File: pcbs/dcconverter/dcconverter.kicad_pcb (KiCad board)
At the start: 4 copper layers, 160 x 100 mm, 52 parts, among them IC1 NCP7805TG, J1 190-9991, J2 Conn_01x01, J3 Conn_01x01, J4 146-8335, J5 Conn_01x01, J6 Conn_01x01, J7 483-8461, J8 483-8461, Q1 NGTB40N120FL2WG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

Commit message: Add power planes
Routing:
- added copper zone on In2.Cu, net Net-(C1-Pad2)
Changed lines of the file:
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@@
+    )
+  )
+  (zone (net 15) (net_name "Net-(F2-Pad1)") (layer In2.Cu) (hatch edge 0.508)
+    (connect_pads (clearance 0.5))
+    (min_thickness 0.25)
+    (fill yes (arc_segments 32) (thermal_gap 0.508) (thermal_bridge_width 0.508) (smoothing chamfer) (radius 1))
+    (polygon
+      (pts
+        (xy 106 77.5) (xy 99 77.5) (xy 99 84) (xy 105 89.5) (xy 130 90)
+        (xy 130 92.5) (xy 133 95.5) (xy 133 108.5) (xy 142 108.5) (xy 146 104.5)
+        (xy 146 93) (xy 151 93) (xy 151 114) (xy 92.5 114) (xy 92.5 71.5)
+        (xy 106 71.5)
+      )
+    )
+  )
+  (zone (net 1) (net_name "Net-(C1-Pad2)") (layer In2.Cu) (hatch edge 0.508)
+    (connect_pads (clearance 0.5))
+    (min_thickness 0.25)
+    (fill yes (arc_segments 32) (thermal_gap 0.508) (thermal_bridge_width 0.508) (smoothing chamfer) (radius 1))
+    (polygon
+      (pts
+        (xy 173.5 61.5) (xy 137.5 61.5) (xy 130 70) (xy 130 88) (xy 105.5 88)
+        (xy 100 83) (xy 100 78) (xy 107.5 78) (xy 107.5 70) (xy 101 70)
+        (xy 101 39.5) (xy 173.5 39.5)
+      )
     )
   )

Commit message: Add power planes
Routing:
- added copper zone on In2.Cu, net Net-(D1-Pad1)
- added copper zone on In2.Cu, net Net-(D5-Pad1)
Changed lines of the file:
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@@
+    )
+  )
+  (zone (net 9) (net_name "Net-(D1-Pad1)") (layer In2.Cu) (hatch edge 0.508)
+    (connect_pads (clearance 0.5))
+    (min_thickness 0.25)
+    (fill yes (arc_segments 32) (thermal_gap 0.508) (thermal_bridge_width 0.508) (smoothing chamfer) (radius 1))
+    (polygon
+      (pts
+        (xy 173.5 17) (xy 173.5 38) (xy 99.5 38) (xy 99.5 70) (xy 91 70)
+        (xy 91 74.5) (xy 82.5 74.5) (xy 82.5 39) (xy 91 39) (xy 91 16.5)
+      )
+    )
+  )
+  (zone (net 12) (net_name "Net-(D5-Pad1)") (layer In2.Cu) (hatch edge 0.508)
+    (connect_pads (clearance 0.5))
+    (min_thickness 0.25)
+    (fill yes (arc_segments 32) (thermal_gap 0.508) (thermal_bridge_width 0.508) (smoothing chamfer) (radius 1))
+    (polygon
+      (pts
+        (xy 90 37.5) (xy 64.5 37.5) (xy 64.5 16.5) (xy 89.5 16.5)
+      )
     )
   )

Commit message: Improve power planes
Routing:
- added copper zone on In1.Cu, net (none)
- added copper zone on In2.Cu, net Net-(C1-Pad1)
- added copper zone on In2.Cu, net Net-(F2-Pad2)
- removed copper zone on In1.Cu, net Net-(C1-Pad2)
- removed copper zone on In2.Cu, net Net-(C1-Pad2)
- removed copper zone on In2.Cu, net Net-(D5-Pad1)
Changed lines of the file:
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@@
     (user_trace_width 5)
     (trace_clearance 0.2)
-    (zone_clearance 0.508)
-    (zone_45_only no)
+    (zone_clearance 0.5)
+    (zone_45_only yes)
     (trace_min 0.2)
     (via_size 0.8)
@@
   (segment (start 15.72501 99.76101) (end 18.647601 102.683601) (width 1) (layer In2.Cu) (net 28))
   (segment (start 15.72501 65.77499) (end 15.72501 99.76101) (width 1) (layer In2.Cu) (net 28))
-  (zone (net 1) (net_name "Net-(C1-Pad2)") (layer In1.Cu) (hatch edge 0.508)
-    (connect_pads (clearance 0.508))
-    (min_thickness 0.254)
+  (zone (net 0) (net_name "") (layer In1.Cu) (hatch edge 0.508)
+    (connect_pads (clearance 0.5))
+    (min_thickness 0.25)
     (fill yes (arc_segments 32) (thermal_gap 0.508) (thermal_bridge_width 0.508) (smoothing chamfer) (radius 1))
     (polygon
       (pts
-        (xy 173.5 17) (xy 174 103) (xy 163 103) (xy 163 114) (xy 27 114)
-        (xy 27 103) (xy 16 103) (xy 16 27) (xy 27 27) (xy 27 16)
-      )
-    )
-  )
-  (zone (net 15) (net_name "Net-(F2-Pad1)") (layer In2.Cu) (hatch edge 0.508)
-    (connect_pads (clearance 0.508))
-    (min_thickness 0.254)
-    (fill yes (arc_segments 32) (thermal_gap 0.508) (thermal_bridge_width 0.508) (smoothing chamfer) (radius 1))
-    (polygon
-      (pts
-        (xy 173.5 64) (xy 174 103) (xy 152.5 103) (xy 152.5 92) (xy 143.5 92)
-        (xy 143.5 105.5) (xy 141 108) (xy 134.5 108) (xy 134.5 95) (xy 131.5 92)
-        (xy 131.5 71) (xy 138 63.5)
+        (xy 163 114) (xy 27 114) (xy 27 103) (xy 16 103) (xy 16 27)
+        (xy 27 27) (xy 27 16) (xy 163 16)
       )
     )
@@
     (polygon
       (pts
-        (xy 106 77.5) (xy 99 77.5) (xy 99 84) (xy 105 89.5) (xy 130 90)
-        (xy 130 92.5) (xy 133 95.5) (xy 133 108.5) (xy 142 108.5) (xy 146 104.5)
-        (xy 146 93) (xy 151 93) (xy 151 114) (xy 92.5 114) (xy 92.5 71.5)
-        (xy 106 71.5)
+        (xy 174 103) (xy 153 103) (xy 153 91) (xy 143.5 91) (xy 143.5 103)
+        (xy 131.5 103) (xy 131.5 67.5) (xy 174 67.5)
       )
     )
   )
-  (zone (net 1) (net_name "Net-(C1-Pad2)") (layer In2.Cu) (hatch edge 0.508)
+  (zone (net 14) (net_name "Net-(F2-Pad2)") (layer In2.Cu) (hatch edge 0.508)
     (connect_pads (clearance 0.5))
     (min_thickness 0.25)
@@
     (polygon
       (pts
-        (xy 173.5 61.5) (xy 137.5 61.5) (xy 130 70) (xy 130 88) (xy 105.5 88)
-        (xy 100 83) (xy 100 78) (xy 107.5 78) (xy 107.5 70) (xy 101 70)
-        (xy 101 39.5) (xy 173.5 39.5)
+        (xy 129.5 105) (xy 144.5 105) (xy 144.5 92.5) (xy 151.5 92.5) (xy 151.5 114)
+        (xy 89 114) (xy 89 92.5) (xy 129.5 92.5)
+      )
+    )
+  )
+  (zone (net 14) (net_name "Net-(F2-Pad2)") (layer In2.Cu) (hatch edge 0.508)
+    (connect_pads (clearance 0.5))
+    (min_thickness 0.25)
+    (fill yes (arc_segments 32) (thermal_gap 0.508) (thermal_bridge_width 0.508) (smoothing chamfer) (radius 1))
+    (polygon
+      (pts
+        (xy 99 83.5) (xy 129.5 83.5) (xy 129.5 92.5) (xy 89 92.5) (xy 89 75.5)
+        (xy 99 75.5)
+      )
+    )
+  )
+  (zone (net 2) (net_name "Net-(C1-Pad1)") (layer In2.Cu) (hatch edge 0.508)
+    (connect_pads (clearance 0.5))
+    (min_thickness 0.25)
+    (fill yes (arc_segments 32) (thermal_gap 0.508) (thermal_bridge_width 0.508) (smoothing chamfer) (radius 1))
+    (polygon
+      (pts
+        (xy 174 66) (xy 130 66) (xy 130 82.5) (xy 105.5 82.5) (xy 105.5 66)
+        (xy 111 60.5) (xy 111 40) (xy 174 40)
       )
     )
@@
     (polygon
       (pts
-        (xy 173.5 17) (xy 173.5 38) (xy 99.5 38) (xy 99.5 70) (xy 91 70)
-        (xy 91 74.5) (xy 82.5 74.5) (xy 82.5 39) (xy 91 39) (xy 91 16.5)
+        (xy 174 38.5) (xy 91.5 38.5) (xy 91.5 16) (xy 174 16)
       )
     )
   )
-  (zone (net 12) (net_name "Net-(D5-Pad1)") (layer In2.Cu) (hatch edge 0.508)
+  (zone (net 9) (net_name "Net-(D1-Pad1)") (layer In2.Cu) (hatch edge 0.508)
     (connect_pads (clearance 0.5))
     (min_thickness 0.25)
@@
     (polygon
       (pts
-        (xy 90 37.5) (xy 64.5 37.5) (xy 64.5 16.5) (xy 89.5 16.5)
+        (xy 104.5 72) (xy 85 72) (xy 85 38.5) (xy 104.5 38.5)
       )
     )
+  )
+  (zone (net 9) (net_name "Net-(D1-Pad1)") (layer In2.Cu) (hatch edge 0.508)
+    (connect_pads (clearance 0.5))
+    (min_thickness 0.25)
+    (fill yes (arc_segments 32) (thermal_gap 0.508) (thermal_bridge_width 0.508) (smoothing chamfer) (radius 1))
+    (polygon
+      (pts
+        (xy 109.5 59.5) (xy 104.5 64.5) (xy 104.5 38.5) (xy 109.5 38.5)
+      )
+    )

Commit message: Improve power planes
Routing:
- net Net-(R12-Pad1): track 126.5 -> 141.6 mm
- added copper zone on In1.Cu, net Net-(C1-Pad2)
- added copper zone on In2.Cu, net Net-(D5-Pad1)
- added copper zone on In2.Cu, net Net-(D5-Pad2)
- added copper zone on In2.Cu, net Net-(F1-Pad2)
- removed copper zone on In1.Cu, net (none)
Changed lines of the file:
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@@
     (thickness 1.6)
     (drawings 4)
-    (tracks 286)
+    (tracks 288)
     (zones 0)
     (modules 52)
@@
   )
   (setup
-    (last_trace_width 2)
+    (last_trace_width 1)
     (user_trace_width 1)
     (user_trace_width 2)
@@
   (segment (start 71.66 33) (end 71.5 33.16) (width 2) (layer B.Cu) (net 28))
   (segment (start 75.5 33) (end 71.66 33) (width 2) (layer B.Cu) (net 28))
-  (segment (start 71.5 33.16) (end 42.66 62) (width 1) (layer In2.Cu) (net 28))
-  (segment (start 19.5 62) (end 15.72501 65.77499) (width 1) (layer In2.Cu) (net 28))
-  (segment (start 42.66 62) (end 19.5 62) (width 1) (layer In2.Cu) (net 28))
   (segment (start 31.016399 102.683601) (end 32.58 101.12) (width 1) (layer In2.Cu) (net 28))
   (segment (start 29.289471 102.683601) (end 31.016399 102.683601) (width 1) (layer In2.Cu) (net 28))
@@
   (segment (start 15.72501 99.76101) (end 18.647601 102.683601) (width 1) (layer In2.Cu) (net 28))
   (segment (start 15.72501 65.77499) (end 15.72501 99.76101) (width 1) (layer In2.Cu) (net 28))
-  (zone (net 0) (net_name "") (layer In1.Cu) (hatch edge 0.508)
+  (segment (start 71.5 33.16) (end 71.5 59) (width 1) (layer In2.Cu) (net 28))
+  (segment (start 55.24227 59) (end 52.74227 61.5) (width 1) (layer In2.Cu) (net 28))
+  (segment (start 71.5 59) (end 55.24227 59) (width 1) (layer In2.Cu) (net 28))
+  (segment (start 20 61.5) (end 15.72501 65.77499) (width 1) (layer In2.Cu) (net 28))
+  (segment (start 52.74227 61.5) (end 20 61.5) (width 1) (layer In2.Cu) (net 28))
+  (zone (net 1) (net_name "Net-(C1-Pad2)") (layer In1.Cu) (hatch edge 0.508)
     (connect_pads (clearance 0.5))
     (min_thickness 0.25)
@@
     (polygon
       (pts
-        (xy 163 114) (xy 27 114) (xy 27 103) (xy 16 103) (xy 16 27)
-        (xy 27 27) (xy 27 16) (xy 163 16)
+        (xy 174 103) (xy 163 103) (xy 163 114) (xy 27 114) (xy 27 103)
+        (xy 16 103) (xy 16 27) (xy 27 27) (xy 27 16) (xy 174 16)
       )
     )
@@
       )
     )
+  )
+  (zone (net 13) (net_name "Net-(F1-Pad2)") (layer In2.Cu) (hatch edge 0.508)
+    (connect_pads (clearance 0.5))
+    (min_thickness 0.25)
+    (fill yes (arc_segments 32) (thermal_gap 0.508) (thermal_bridge_width 0.508) (smoothing chamfer) (radius 1))
+    (polygon
+      (pts
+        (xy 47.5 59.5) (xy 16 59.5) (xy 16 27) (xy 27 27) (xy 27 16)
+        (xy 47.5 16)
+      )
+    )
+  )
+  (zone (net 12) (net_name "Net-(D5-Pad1)") (layer In2.Cu) (hatch edge 0.508)
+    (connect_pads (clearance 0.5))
+    (min_thickness 0.25)
+    (fill yes (arc_segments 32) (thermal_gap 0.508) (thermal_bridge_width 0.508) (smoothing chamfer) (radius 1))
+    (polygon
+      (pts
+        (xy 90 37) (xy 61.5 37) (xy 61.5 16) (xy 90 16)
+      )
+    )
+  )
+  (zone (net 11) (net_name "Net-(D5-Pad2)") (layer In2.Cu) (hatch edge 0.508)
+    (connect_pads (clearance 0.5))
+    (min_thickness 0.25)
+    (fill yes (arc_segments 32) (thermal_gap 0.508) (thermal_bridge_width 0.508) (smoothing chamfer) (radius 1))
+    (polygon
+      (pts
+        (xy 60 37) (xy 49 37) (xy 49 16) (xy 60 16)
+      )
+    )

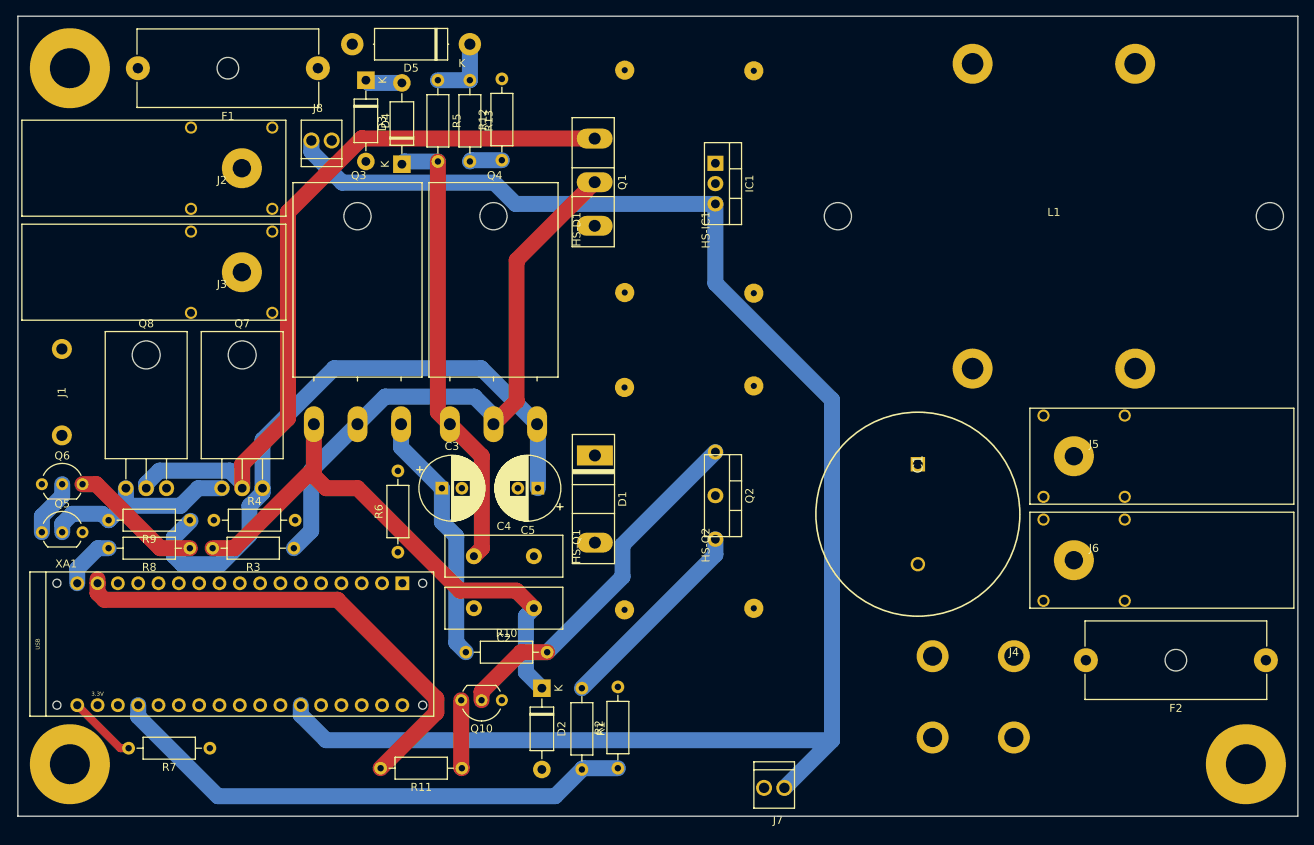
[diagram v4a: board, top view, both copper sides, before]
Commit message: Update Plot for DC Converter
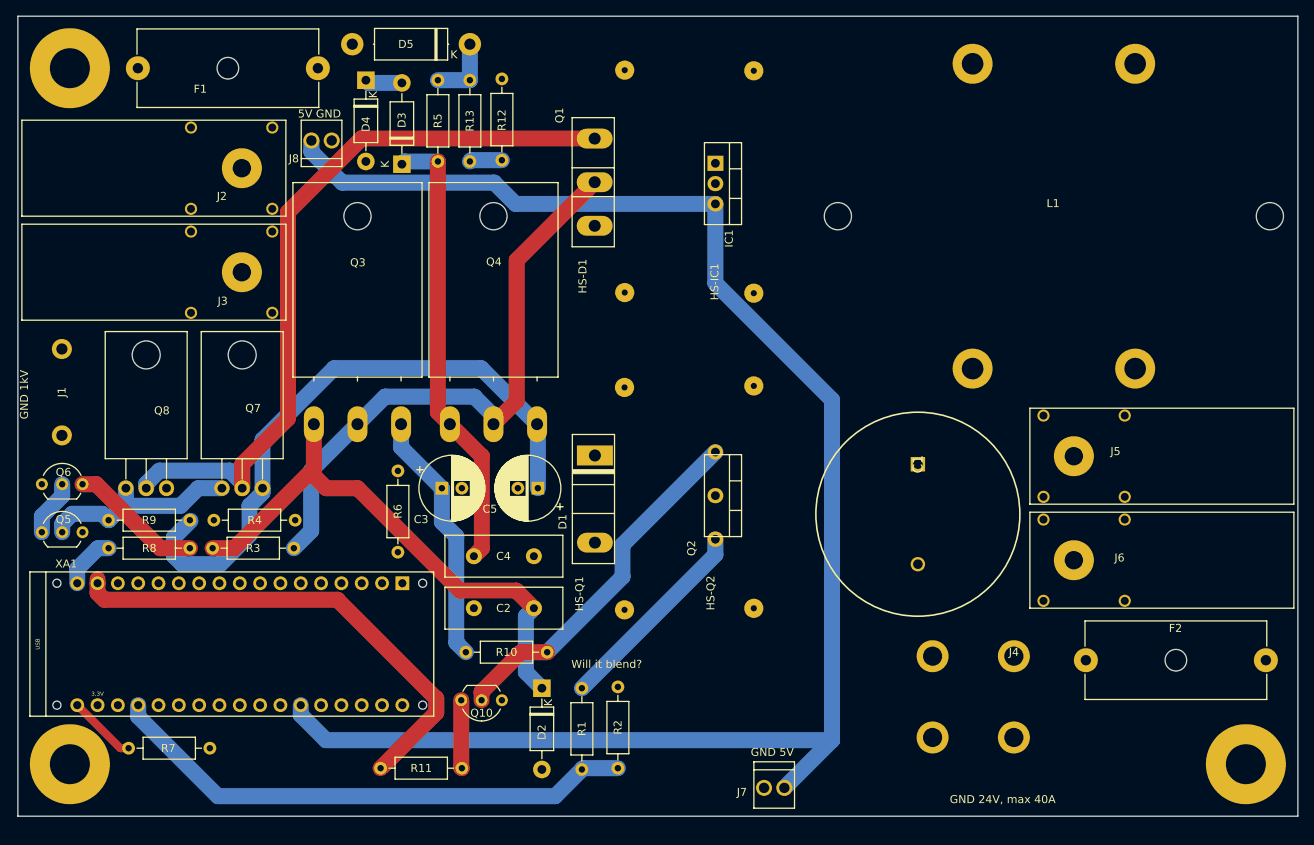
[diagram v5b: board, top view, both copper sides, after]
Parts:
- F2: value 25A -> 40A
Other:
- board text added: "5V GND"
- board text added: "GND 1kV"
- board text added: "GND 24V, max 40A"
- board text added: "GND 5V"
- board text added: "Will it blend?"
